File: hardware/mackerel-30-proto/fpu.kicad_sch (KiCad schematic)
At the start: 1 part, among them U10 MC68882

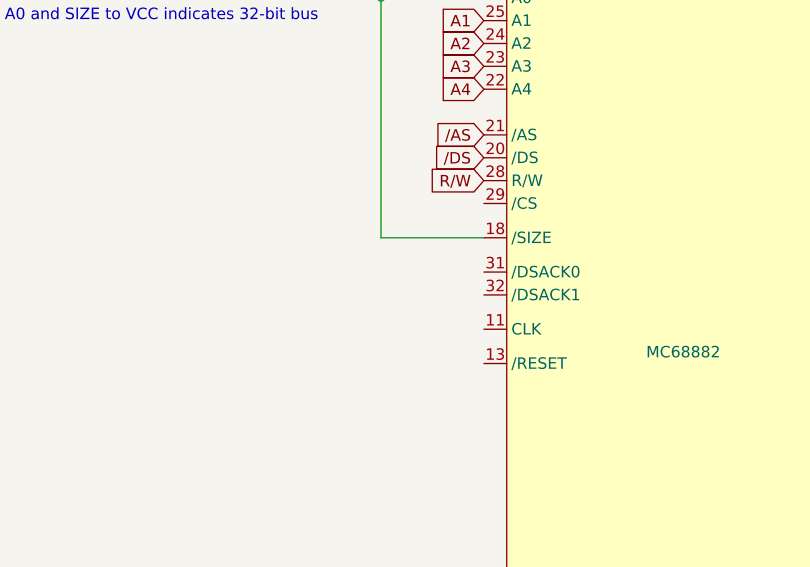
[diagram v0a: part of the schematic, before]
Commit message: Wired most of the control signals for the CPU and DRAM
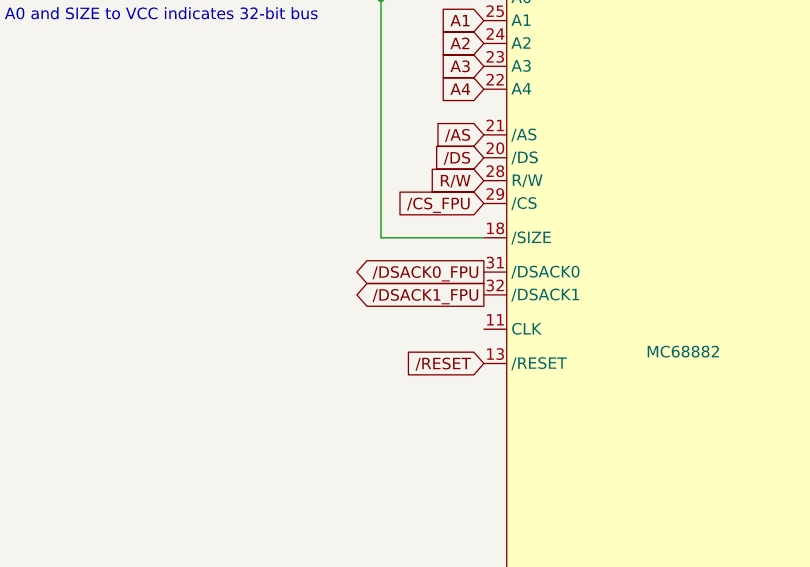
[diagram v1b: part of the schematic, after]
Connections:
- net /RESET: now reaches U10.13 (/RESET)
- net /CS_FPU: now reaches U10.29 (/CS)
- net /DSACK0_FPU: now reaches U10.31 (/DSACK0)
- net /DSACK1_FPU: now reaches U10.32 (/DSACK1)
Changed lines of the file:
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@@
+		)
+	)
+	(global_label "{slash}RESET"
+		(shape input)
+		(at 72.39 97.79 180)
+		(fields_autoplaced yes)
+		(effects
+			(font
+				(size 1.27 1.27)
+			)
+			(justify right)
+		)
+		(property "Intersheetrefs" "${INTERSHEET_REFS}"
+			(at 62.3292 97.79 0)
+			(effects
+				(font
+					(size 1.27 1.27)
+				)
+				(justify right)
+				(hide yes)
+			)
 		)
 	)
@@
 		)
 	)
+	(global_label "{slash}CS_FPU"
+		(shape input)
+		(at 72.39 80.01 180)
+		(fields_autoplaced yes)
+		(effects
+			(font
+				(size 1.27 1.27)
+			)
+			(justify right)
+		)
+		(property "Intersheetrefs" "${INTERSHEET_REFS}"
+			(at 60.9381 80.01 0)
+			(effects
+				(font
+					(size 1.27 1.27)
+				)
+				(justify right)
+				(hide yes)
+			)
+		)
+	)
 	(global_label "D2"
 		(shape bidirectional)
@@
 		)
 	)
+	(global_label "{slash}DSACK1_FPU"
+		(shape output)
+		(at 72.39 90.17 180)
+		(fields_autoplaced yes)
+		(effects
+			(font
+				(size 1.27 1.27)
+			)
+			(justify right)
+		)
+		(property "Intersheetrefs" "${INTERSHEET_REFS}"
+			(at 56.1 90.17 0)
+			(effects
+				(font
+					(size 1.27 1.27)
+				)
+				(justify right)
+				(hide yes)
+			)
+		)
+	)
 	(global_label "D22"
 		(shape bidirectional)
@@
 		(property "Intersheetrefs" "${INTERSHEET_REFS}"
 			(at 65.7762 72.39 0)
+			(effects
+				(font
+					(size 1.27 1.27)
+				)
+				(justify right)
+				(hide yes)
+			)
+		)
+	)
+	(global_label "{slash}DSACK0_FPU"
+		(shape output)
+		(at 72.39 87.63 180)
+		(fields_autoplaced yes)
+		(effects
+			(font
+				(size 1.27 1.27)
+			)
+			(justify right)
+		)
+		(property "Intersheetrefs" "${INTERSHEET_REFS}"
+			(at 56.1 87.63 0)
 			(effects
 				(font
@@
 		(dnp no)
 		(fields_autoplaced yes)
-		(property "Reference" "#PWR049"
+		(property "Reference" "#PWR053"
 			(at 60.96 58.42 0)
 			(effects
@@
 			(project ""
 				(path "/9307474f-ec99-494d-b4c9-fbd0b10ce86a/a9f13681-faa6-4706-8ec9-421e908e3ee4"
-					(reference "#PWR049")
+					(reference "#PWR053")
 					(unit 1)
 				)
@@
 		(dnp no)
 		(fields_autoplaced yes)
-		(property "Reference" "#PWR048"
+		(property "Reference" "#PWR055"
 			(at 107.95 147.32 0)
 			(effects
@@
 			(project ""
 				(path "/9307474f-ec99-494d-b4c9-fbd0b10ce86a/a9f13681-faa6-4706-8ec9-421e908e3ee4"
-					(reference "#PWR048")
+					(reference "#PWR055")
 					(unit 1)
 				)
@@
 		(dnp no)
 		(fields_autoplaced yes)
-		(property "Reference" "#PWR047"
+		(property "Reference" "#PWR054"
 			(at 85.09 52.07 0)
 			(effects
@@
 			(project ""
 				(path "/9307474f-ec99-494d-b4c9-fbd0b10ce86a/a9f13681-faa6-4706-8ec9-421e908e3ee4"
-					(reference "#PWR047")
+					(reference "#PWR054")
 					(unit 1)
 				)

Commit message: positioning
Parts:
- renumbered U10 to U11
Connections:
- net CLK_CPU: now reaches U11.11 (CLK)
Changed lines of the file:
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@@
+		)
+	)
+	(global_label "CLK_CPU"
+		(shape input)
+		(at 72.39 93.98 180)
+		(fields_autoplaced yes)
+		(effects
+			(font
+				(size 1.27 1.27)
+			)
+			(justify right)
+		)
+		(property "Intersheetrefs" "${INTERSHEET_REFS}"
+			(at 60.9986 93.98 0)
+			(effects
+				(font
+					(size 1.27 1.27)
+				)
+				(justify right)
+				(hide yes)
+			)
 		)
 	)
@@
 		(dnp no)
 		(fields_autoplaced yes)
-		(property "Reference" "#PWR049"
+		(property "Reference" "#PWR070"
 			(at 60.96 58.42 0)
 			(effects
@@
 			(project ""
 				(path "/9307474f-ec99-494d-b4c9-fbd0b10ce86a/a9f13681-faa6-4706-8ec9-421e908e3ee4"
-					(reference "#PWR049")
+					(reference "#PWR070")
 					(unit 1)
 				)
@@
 		(on_board yes)
 		(dnp no)
-		(property "Reference" "U10"
+		(property "Reference" "U11"
 			(at 108.966 48.768 0)
 			(effects
@@
 			(project ""
 				(path "/9307474f-ec99-494d-b4c9-fbd0b10ce86a/a9f13681-faa6-4706-8ec9-421e908e3ee4"
-					(reference "U10")
+					(reference "U11")
 					(unit 1)
 				)
@@
 		(dnp no)
 		(fields_autoplaced yes)
-		(property "Reference" "#PWR051"
+		(property "Reference" "#PWR072"
 			(at 107.95 147.32 0)
 			(effects
@@
 			(project ""
 				(path "/9307474f-ec99-494d-b4c9-fbd0b10ce86a/a9f13681-faa6-4706-8ec9-421e908e3ee4"
-					(reference "#PWR051")
+					(reference "#PWR072")
 					(unit 1)
 				)
@@
 		(dnp no)
 		(fields_autoplaced yes)
-		(property "Reference" "#PWR050"
+		(property "Reference" "#PWR071"
 			(at 85.09 52.07 0)
 			(effects
@@
 			(project ""
 				(path "/9307474f-ec99-494d-b4c9-fbd0b10ce86a/a9f13681-faa6-4706-8ec9-421e908e3ee4"
-					(reference "#PWR050")
+					(reference "#PWR071")
 					(unit 1)
 				)

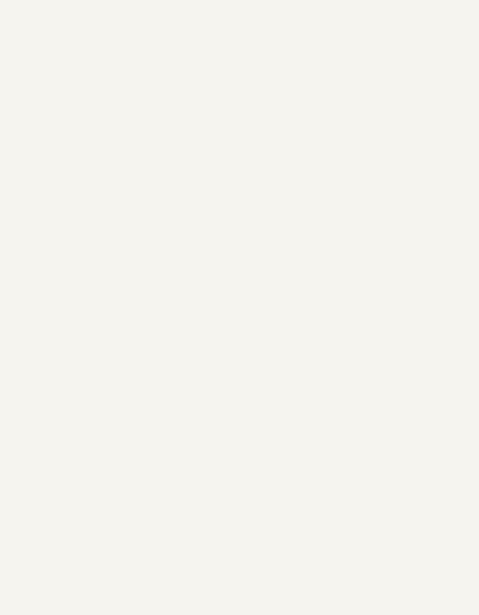
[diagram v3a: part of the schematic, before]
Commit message: Mostly fixed the SIMM-72 footprint
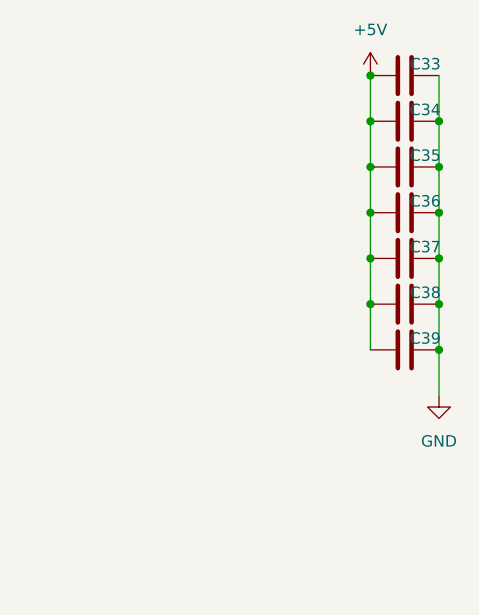
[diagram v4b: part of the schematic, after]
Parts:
- added C33, C34, C35, C36, C37, C38, C39: 0.1uF, Capacitor_SMD:C_1206_3216Metric_Pad1.33x1.80mm_HandSolder, symbol Device:C
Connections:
- net +5V: now also C33.1, C34.1, C35.1, C36.1, C37.1, C38.1, C39.1
- net GND: now also C33.2, C34.2, C35.2, C36.2, C37.2, C38.2, C39.2

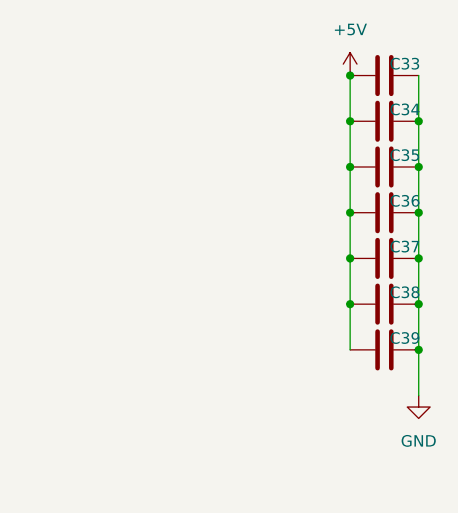
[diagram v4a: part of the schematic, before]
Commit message: Add DS1233 for reset
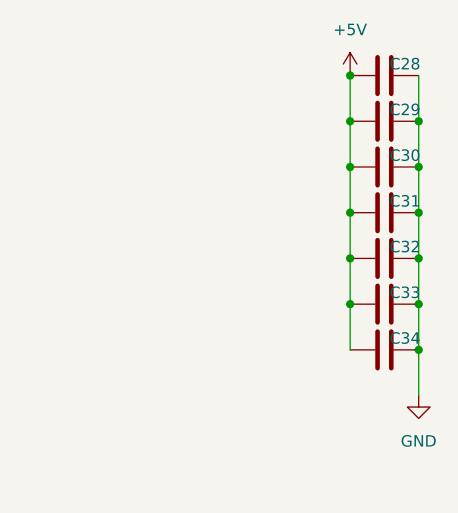
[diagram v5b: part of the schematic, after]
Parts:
- renumbered C33 to C28, C34 to C29, C35 to C30, C36 to C31, C37 to C32, C38 to C33, C39 to C34

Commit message: rough layout of the PCB components
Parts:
- C28, C29, C30, C31, C32, C33, C34: footprint Capacitor_SMD:C_1206_3216Metric_Pad1.33x1.80mm_HandSolder -> Capacitor_THT:C_Disc_D4.3mm_W1.9mm_P5.00mm
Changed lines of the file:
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@@
 			)
 		)
-		(property "Footprint" "Capacitor_SMD:C_1206_3216Metric_Pad1.33x1.80mm_HandSolder"
+		(property "Footprint" "Capacitor_THT:C_Disc_D4.3mm_W1.9mm_P5.00mm"
 			(at 186.69 39.6748 0)
 			(effects
@@
 			)
 		)
-		(property "Footprint" "Capacitor_SMD:C_1206_3216Metric_Pad1.33x1.80mm_HandSolder"
+		(property "Footprint" "Capacitor_THT:C_Disc_D4.3mm_W1.9mm_P5.00mm"
 			(at 186.69 54.9148 0)
 			(effects
@@
 			)
 		)
-		(property "Footprint" "Capacitor_SMD:C_1206_3216Metric_Pad1.33x1.80mm_HandSolder"
+		(property "Footprint" "Capacitor_THT:C_Disc_D4.3mm_W1.9mm_P5.00mm"
 			(at 186.69 59.9948 0)
 			(effects
@@
 			)
 		)
-		(property "Footprint" "Capacitor_SMD:C_1206_3216Metric_Pad1.33x1.80mm_HandSolder"
+		(property "Footprint" "Capacitor_THT:C_Disc_D4.3mm_W1.9mm_P5.00mm"
 			(at 186.69 44.7548 0)
 			(effects
@@
 			)
 		)
-		(property "Footprint" "Capacitor_SMD:C_1206_3216Metric_Pad1.33x1.80mm_HandSolder"
+		(property "Footprint" "Capacitor_THT:C_Disc_D4.3mm_W1.9mm_P5.00mm"
 			(at 186.69 34.5948 0)
 			(effects
@@
 			)
 		)
-		(property "Footprint" "Capacitor_SMD:C_1206_3216Metric_Pad1.33x1.80mm_HandSolder"
+		(property "Footprint" "Capacitor_THT:C_Disc_D4.3mm_W1.9mm_P5.00mm"
 			(at 186.69 49.8348 0)
 			(effects
@@
 			)
 		)
-		(property "Footprint" "Capacitor_SMD:C_1206_3216Metric_Pad1.33x1.80mm_HandSolder"
+		(property "Footprint" "Capacitor_THT:C_Disc_D4.3mm_W1.9mm_P5.00mm"
 			(at 186.69 65.0748 0)
 			(effects

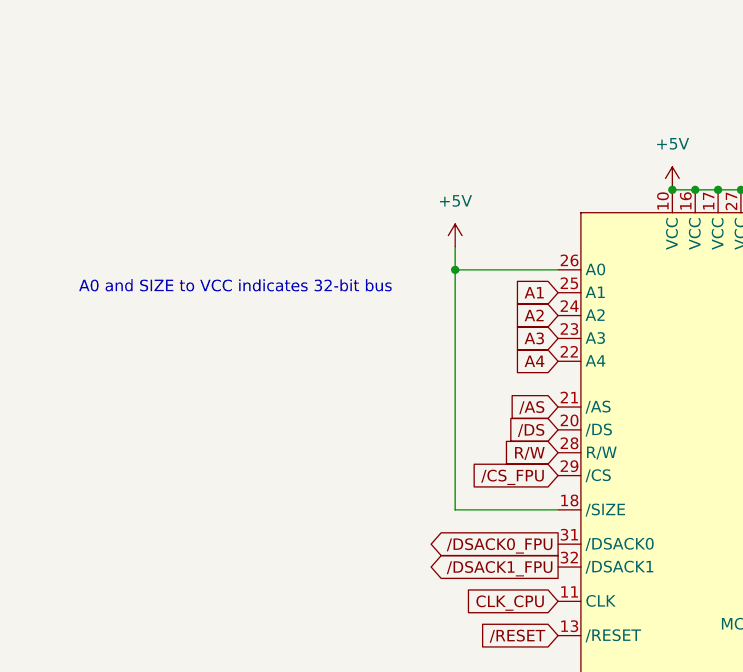
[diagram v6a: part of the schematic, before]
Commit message: Routed DUART serial and GPIO
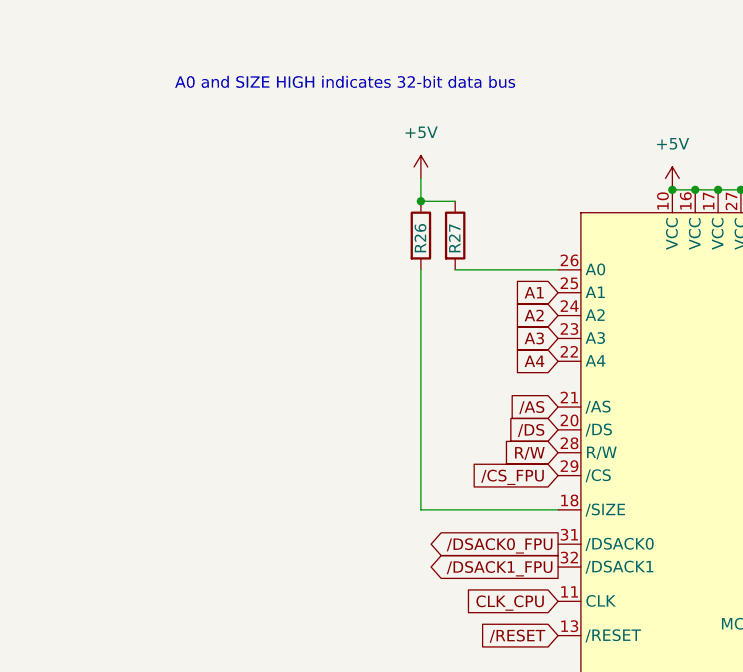
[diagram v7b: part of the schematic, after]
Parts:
- added R26, R27: 4k7, Resistor_THT:R_Axial_DIN0207_L6.3mm_D2.5mm_P7.62mm_Horizontal, symbol Device:R
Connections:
- net +5V: now also R26.1, R27.1; no longer U11.18 (/SIZE), U11.26 (A0)
- new net: R27.2, U11.26 (A0)
- new net: R26.2, U11.18 (/SIZE)
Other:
- note added: "A0 and SIZE HIGH indicates 32-bit data bus"
- note removed: "A0 and SIZE to VCC indicates 32-bit bus"
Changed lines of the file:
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@@
+	)
+	(junction
+		(at 57.15 49.53)
+		(diameter 0)
+		(color 0 0 0 0)
 	)
 	(junction
@@
 	)
 	(junction
-		(at 60.96 57.15)
-		(diameter 0)
-		(color 0 0 0 0)
-	)
-	(junction
 		(at 87.63 140.97)
 		(diameter 0)
@@
 	(wire
 		(pts
+			(xy 102.87 140.97) (xy 105.41 140.97)
+		)
+		(stroke
+			(width 0)
+			(type default)
+		)
+	)
+	(wire
+		(pts
+			(xy 90.17 48.26) (xy 92.71 48.26)
+		)
+		(stroke
+			(width 0)
+			(type default)
+		)
+	)
+	(wire
+		(pts
+			(xy 87.63 48.26) (xy 90.17 48.26)
+		)
+		(stroke
+			(width 0)
+			(type default)
+		)
+	)
+	(wire
+		(pts
+			(xy 186.69 45.72) (xy 186.69 50.8)
+		)
+		(stroke
+			(width 0)
+			(type default)
+		)
+	)
+	(wire
+		(pts
+			(xy 179.07 45.72) (xy 179.07 50.8)
+		)
+		(stroke
+			(width 0)
+			(type default)
+		)
+	)
+	(wire
+		(pts
+			(xy 82.55 140.97) (xy 85.09 140.97)
+		)
+		(stroke
+			(width 0)
+			(type default)
+		)
+	)
+	(wire
+		(pts
+			(xy 57.15 49.53) (xy 60.96 49.53)
+		)
+		(stroke
+			(width 0)
+			(type default)
+		)
+	)
+	(wire
+		(pts
+			(xy 72.39 140.97) (xy 80.01 140.97)
+		)
+		(stroke
+			(width 0)
+			(type default)
+		)
+	)
+	(wire
+		(pts
 			(xy 60.96 57.15) (xy 72.39 57.15)
 		)
@@
 	(wire
 		(pts
-			(xy 102.87 140.97) (xy 105.41 140.97)
-		)
-		(stroke
-			(width 0)
-			(type default)
-		)
-	)
-	(wire
-		(pts
-			(xy 90.17 48.26) (xy 92.71 48.26)
-		)
-		(stroke
-			(width 0)
-			(type default)
-		)
-	)
-	(wire
-		(pts
-			(xy 87.63 48.26) (xy 90.17 48.26)
-		)
-		(stroke
-			(width 0)
-			(type default)
-		)
-	)
-	(wire
-		(pts
-			(xy 186.69 45.72) (xy 186.69 50.8)
-		)
-		(stroke
-			(width 0)
-			(type default)
-		)
-	)
-	(wire
-		(pts
-			(xy 179.07 45.72) (xy 179.07 50.8)
-		)
-		(stroke
-			(width 0)
-			(type default)
-		)
-	)
-	(wire
-		(pts
-			(xy 82.55 140.97) (xy 85.09 140.97)
-		)
-		(stroke
-			(width 0)
-			(type default)
-		)
-	)
-	(wire
-		(pts
-			(xy 72.39 140.97) (xy 80.01 140.97)
+			(xy 57.15 83.82) (xy 57.15 57.15)
 		)
 		(stroke
@@
 	(wire
 		(pts
-			(xy 72.39 83.82) (xy 60.96 83.82)
-		)
-		(stroke
-			(width 0)
-			(type default)
-		)
-	)
-	(wire
-		(pts
-			(xy 60.96 54.61) (xy 60.96 57.15)
+			(xy 57.15 83.82) (xy 72.39 83.82)
+		)
+		(stroke
+			(width 0)
+			(type default)
+		)
+	)
+	(wire
+		(pts
+			(xy 57.15 46.99) (xy 57.15 49.53)
 		)
 		(stroke
@@
 	(wire
 		(pts
-			(xy 60.96 83.82) (xy 60.96 57.15)
-		)
-		(stroke
-			(width 0)
-			(type default)
-		)
-	)
-	(wire
-		(pts
 			(xy 179.07 40.64) (xy 179.07 45.72)
 		)
@@
 		)
 	)
-	(text "A0 and SIZE to VCC indicates 32-bit bus"
+	(text "A0 and SIZE HIGH indicates 32-bit data bus"
 		(exclude_from_sim no)
-		(at 36.576 59.182 0)
+		(at 48.768 36.576 0)
 		(effects
 			(font
@@
 	(symbol
 		(lib_id "power:+5V")
-		(at 60.96 54.61 0)
+		(at 57.15 46.99 0)
 		(unit 1)
 		(exclude_from_sim no)
@@
 		(fields_autoplaced yes)
 		(property "Reference" "#PWR068"
-			(at 60.96 58.42 0)
+			(at 57.15 50.8 0)
 			(effects
 				(font
@@
 		)
 		(property "Value" "+5V"
-			(at 60.96 49.53 0)
+			(at 57.15 41.91 0)
 			(effects
 				(font
@@
 		)
 		(property "Footprint" ""
-			(at 60.96 54.61 0)
+			(at 57.15 46.99 0)
 			(effects
 				(font
@@
 		)
 		(property "Datasheet" ""
-			(at 60.96 54.61 0)
+			(at 57.15 46.99 0)
 			(effects
 				(font
@@
 		)
 		(property "Description" "Power symbol creates a global label with name \"+5V\""
-			(at 60.96 54.61 0)
+			(at 57.15 46.99 0)
 			(effects
 				(font
@@
 	)
 	(symbol
+		(lib_id "Device:R")
+		(at 60.96 53.34 0)
+		(unit 1)
+		(exclude_from_sim no)
+		(in_bom yes)
+		(on_board yes)
+		(dnp no)
+		(property "Reference" "R27"
+			(at 60.96 55.372 90)
+			(effects
+				(font
+					(size 1.27 1.27)
+				)
+				(justify left)
+			)
+		)
+		(property "Value" "4k7"
+			(at 60.96 55.118 90)
+			(effects
+				(font
+					(size 1.27 1.27)
+				)
+				(justify left)
+				(hide yes)
+			)
+		)
+		(property "Footprint" "Resistor_THT:R_Axial_DIN0207_L6.3mm_D2.5mm_P7.62mm_Horizontal"
+			(at 59.182 53.34 90)
+			(effects
+				(font
+					(size 1.27 1.27)
+				)
+				(hide yes)
+			)
+		)
+		(property "Datasheet" "~"
+			(at 60.96 53.34 0)
+			(effects
+				(font
+					(size 1.27 1.27)
+				)
+				(hide yes)
+			)
+		)
+		(property "Description" "Resistor"
+			(at 60.96 53.34 0)
+			(effects
+				(font
+					(size 1.27 1.27)
+				)
+				(hide yes)
+			)
+		)
+		(pin "2"
+		)
+		(pin "1"
+		)
+		(instances
+			(project "mackerel-30-proto"
+				(path "/9307474f-ec99-494d-b4c9-fbd0b10ce86a/a9f13681-faa6-4706-8ec9-421e908e3ee4"
+					(reference "R27")
+					(unit 1)
+				)
+			)
+		)
+	)
+	(symbol
 		(lib_id "mackerel-68k-symbols:MC68882")
 		(at 93.98 96.52 0)
@@
 					(unit 1)
 				)
+			)
+		)
+	)
+	(symbol
+		(lib_id "Device:R")
+		(at 57.15 53.34 0)
+		(unit 1)
+		(exclude_from_sim no)
+		(in_bom yes)
+		(on_board yes)
+		(dnp no)
+		(property "Reference" "R26"
+			(at 57.15 55.372 90)
+			(effects
+				(font
+					(size 1.27 1.27)
+				)
+				(justify left)
+			)
+		)
+		(property "Value" "4k7"
+			(at 57.15 55.118 90)
+			(effects
+				(font
+					(size 1.27 1.27)
+				)
+				(justify left)
+				(hide yes)
+			)
+		)
+		(property "Footprint" "Resistor_THT:R_Axial_DIN0207_L6.3mm_D2.5mm_P7.62mm_Horizontal"
+			(at 55.372 53.34 90)
+			(effects
+				(font
+					(size 1.27 1.27)
+				)
+				(hide yes)
+			)
+		)
+		(property "Datasheet" "~"
+			(at 57.15 53.34 0)
+			(effects
+				(font
+					(size 1.27 1.27)
+				)
+				(hide yes)
+			)
+		)
+		(property "Description" "Resistor"
+			(at 57.15 53.34 0)
+			(effects
+				(font
+					(size 1.27 1.27)
+				)
+				(hide yes)
+			)
+		)
+		(pin "2"
+		)
+		(pin "1"
+		)
+		(instances
+			(project "mackerel-30-proto"
+				(path "/9307474f-ec99-494d-b4c9-fbd0b10ce86a/a9f13681-faa6-4706-8ec9-421e908e3ee4"
+					(reference "R26")
+					(unit 1)
+				)
